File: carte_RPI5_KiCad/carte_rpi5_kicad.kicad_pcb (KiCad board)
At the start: 2 copper layers, 134.6 x 58.9 mm, 26 parts, among them J1 Conn_01x03, J10 RPI5_40pins, J2 Conn_01x03, J3 Conn_01x03, J4 Conn_01x03, J5 Conn_01x03, J6 Conn_01x03, J7 Conn_01x03, J8 Conn_01x03, J9 XT60-M, SW1 SW_SPDT

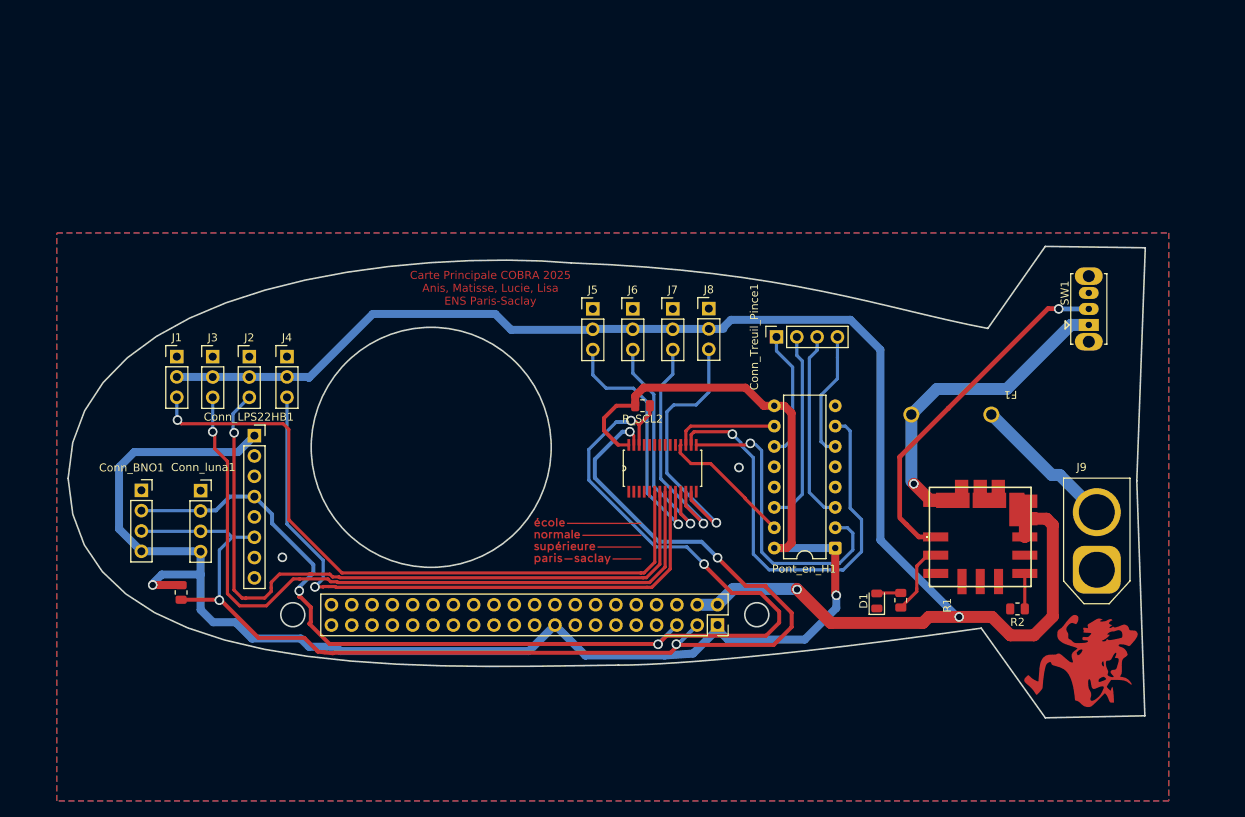
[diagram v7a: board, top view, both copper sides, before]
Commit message: changement_sens_connecteur_RPI
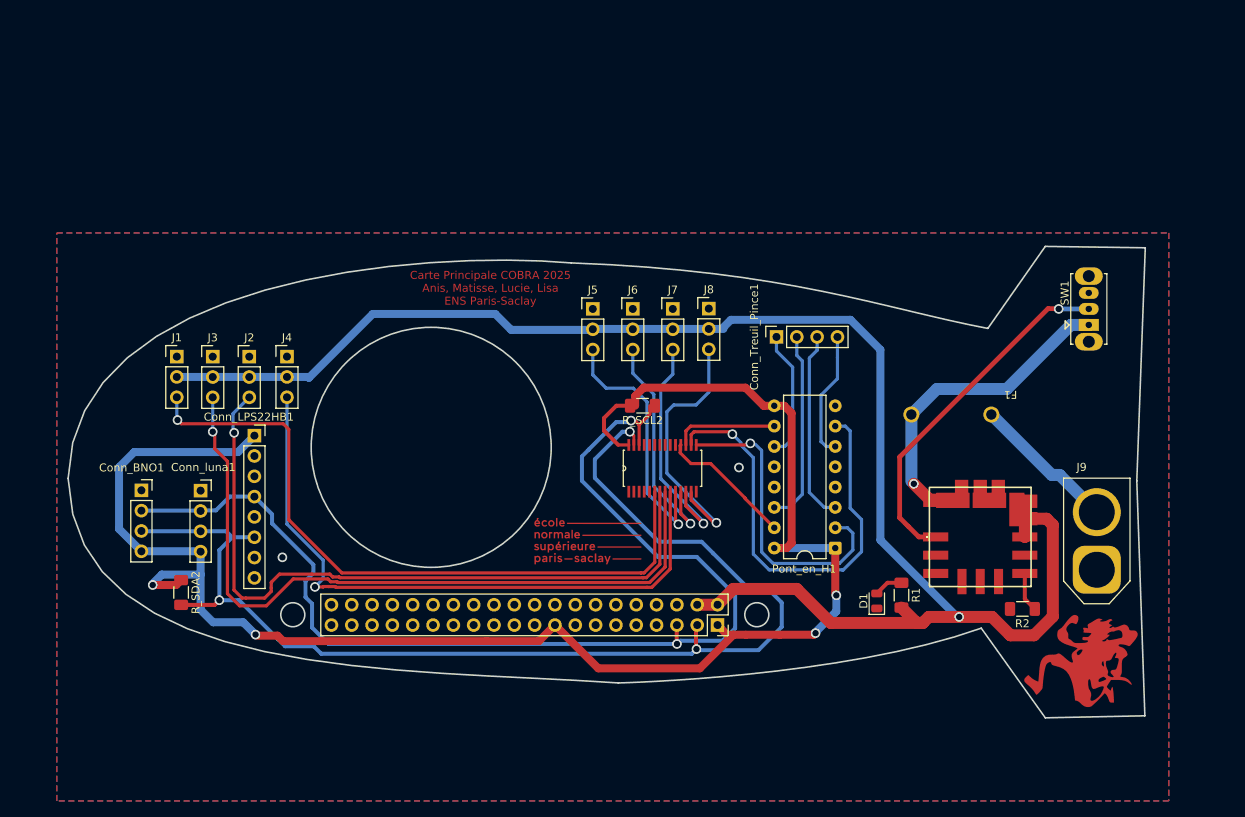
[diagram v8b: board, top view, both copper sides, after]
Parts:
- R1, R2, R_SCL2, R_SDA2: footprint Resistor_SMD:R_0805_2012Metric -> Resistor_SMD:R_1206_3216Metric_Pad1.30x1.75mm_HandSolder
- moved R1 0.64 mm to (166.6, 105.3)
- moved R2 0.61 mm to (181.7, 107.0)
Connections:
- R1 pad 2: Net-(Régulateur_de_tension1-POWER_GOOD_OUT) -> 5V
- Régulateur_de_tension1 pad 10: Net-(Régulateur_de_tension1-POWER_GOOD_OUT) -> unconnected-(Régulateur_de_tension1-POWER_GOOD_OUT-Pad10)
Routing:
- net SCL: track 151.2 -> 141.8 mm, vias 4 -> 2
- net Net-(Régulateur_de_tension1-POWER_GOOD_OUT): track 8.94 -> 0.00 mm
- net 5V: track 201.3 -> 204.7 mm, vias 2 -> 1
- net SDA: track 150.8 -> 152.5 mm, vias 4 -> 3
- net unconnected-(Régulateur_de_tension1-POWER_GOOD_OUT-Pad10): track 0.00 -> 1.01 mm
- net 3.3V: track 211.8 -> 212.8 mm, vias 2 -> 4
- net Net-(D1-A): track 3.03 -> 3.63 mm
- net Net-(Régulateur_de_tension1-TRIM): track 4.44 -> 4.95 mm
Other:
- outline, holes or cut-outs redrawn
